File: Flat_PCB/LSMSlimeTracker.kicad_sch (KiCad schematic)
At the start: 49 parts, among them J1 USB_C_Receptacle_USB2.0, J2 Conn_01x04_Socket, Q1 Q_PMOS_GSD, SW1 SW_Push, SW2 SW_SPDT, SW3 SW_Push, U1 LSM6DSV16X, U2 M3406, U3 ESP32-C3-WROOM-02-N4, U7 BQ24040DSQT

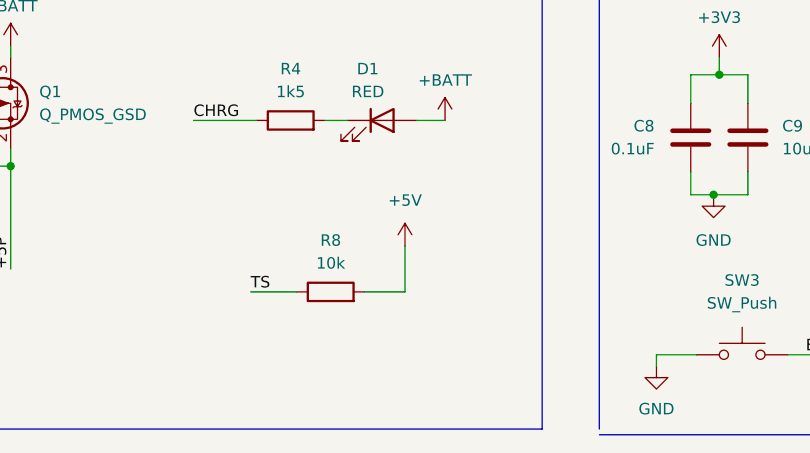
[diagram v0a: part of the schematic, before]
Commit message: TTDM fix
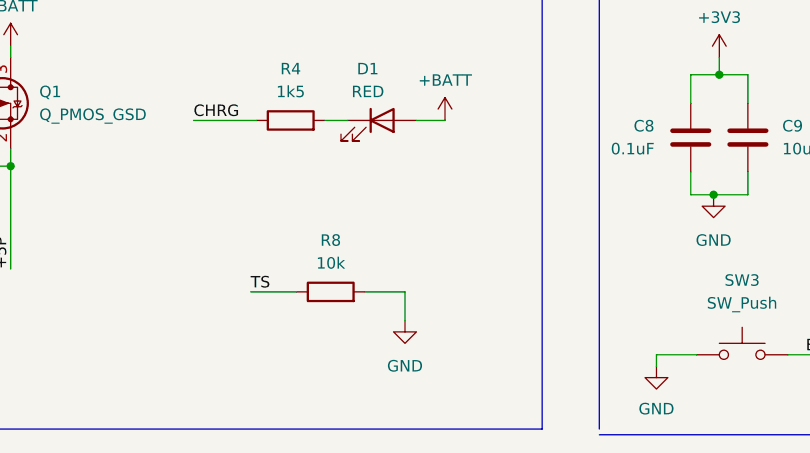
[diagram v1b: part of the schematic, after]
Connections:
- net +5V: no longer R8.2
- net GND: now also R8.2
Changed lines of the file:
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@@
-    (stroke (width 0) (type default))
-  )
-  (wire (pts (xy 196.85 180.34) (xy 196.85 185.42))
     (stroke (width 0) (type default))
   )
@@
   )
   (polyline (pts (xy 212.09 200.66) (xy 212.09 17.78))
+    (stroke (width 0) (type default))
+  )
+  (wire (pts (xy 196.85 185.42) (xy 196.85 188.595))
     (stroke (width 0) (type default))
   )
@@
         (path "/c06b72f6-429a-4daf-bf10-b679f7f09670"
           (reference "#PWR021") (unit 1)
-        )
-      )
-    )
-  )
-  (symbol (lib_id "power:+5V") (at 196.85 180.34 0) (unit 1)
-    (in_bom yes) (on_board yes) (dnp no) (fields_autoplaced)
-    (property "Reference" "#PWR017" (at 196.85 184.15 0)
-      (effects (font (size 1.27 1.27)) hide)
-    )
-    (property "Value" "+5V" (at 196.85 175.26 0)
-      (effects (font (size 1.27 1.27)))
-    )
-    (property "Footprint" "" (at 196.85 180.34 0)
-      (effects (font (size 1.27 1.27)) hide)
-    )
-    (property "Datasheet" "" (at 196.85 180.34 0)
-      (effects (font (size 1.27 1.27)) hide)
-    )
-    (pin "1")
-    (instances
-      (project "LSMSlimeTracker"
-        (path "/c06b72f6-429a-4daf-bf10-b679f7f09670"
-          (reference "#PWR017") (unit 1)
         )
       )
@@
         )
       )
+    )
+  )
+  (symbol (lib_id "power:GND") (at 196.85 188.595 0) (unit 1)
+    (in_bom yes) (on_board yes) (dnp no) (fields_autoplaced)
+    (property "Reference" "#PWR017" (at 196.85 194.945 0)
+      (effects (font (size 1.27 1.27)) hide)
+    )
+    (property "Value" "GND" (at 196.85 193.675 0)
+      (effects (font (size 1.27 1.27)))
+    )
+    (property "Footprint" "" (at 196.85 188.595 0)
+      (effects (font (size 1.27 1.27)) hide)
+    )
+    (property "Datasheet" "" (at 196.85 188.595 0)
+      (effects (font (size 1.27 1.27)) hide)
+    )
+    (pin "1")
+    (instances
+      (project "LSMSlimeTracker"
+        (path "/c06b72f6-429a-4daf-bf10-b679f7f09670"
+          (reference "#PWR017") (unit 1)
+        )
+      )

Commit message: V1.2
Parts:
- removed C4: 4.7uF, Capacitor_SMD:C_0603_1608Metric, symbol Device:C
- removed R1, R21: 10k, Resistor_SMD:R_0603_1608Metric, symbol Device:R
- removed R12: 100k, Resistor_SMD:R_0603_1608Metric, symbol Device:R
- removed R13: 180k, Resistor_SMD:R_0603_1608Metric, symbol Device:R
- removed R20, R22: 5k1, Resistor_SMD:R_0603_1608Metric, symbol Device:R
- removed R4: 1k5, Resistor_SMD:R_0603_1608Metric, symbol Device:R
- added C6: 10uF, Capacitor_SMD:C_0603_1608Metric, symbol Device:C
- added R10, R15, R17: 150k, Resistor_SMD:R_0603_1608Metric, symbol Device:R
- added R14, R16, R18, R6: 10k, Resistor_SMD:R_0603_1608Metric, symbol Device:R
- added R9: 2k, Resistor_SMD:R_0603_1608Metric, symbol Device:R
- R11: value 220k -> 150k; MPN C25767 -> C25755
- R5: value 1k5 -> 150k; MPN C25867 -> C25755
- R7: value 100k -> 2k; MPN C25741 -> C4109
- R8: value 10k -> 5k1; MPN C25744 -> C25905
- TP1: renamed from TP2; now left out of the parts list
- TP2: renamed from TP1; now left out of the parts list
- TP3: renamed from TP7; now left out of the parts list
- TP4: renamed from TP5; now left out of the parts list
- TP5: renamed from TP6; now left out of the parts list
- TP6: renamed from TP3; now left out of the parts list
- TP7: renamed from TP4; now left out of the parts list
- U1: footprint LGA_Custom:LGA14L_LSM6_STM -> LGA_Custom:Bosch_LGA-14_3x2.5mm_P0.5mm
- U2: renamed from U7; footprint SON40P200X200X80-11N -> SON_Custom:SON40P200X200X80-11N
- U3: footprint MODULE_ESP32-C3-WROOM-02-H4 -> ESP_Custom:MODULE_ESP32-C3-WROOM-02-H4
- renumbered C2 to C1, C1 to C2, C11 to C3, C12 to C4, C8 to C5, C9 to C7, C3 to C8, C5 to C9, D2 to D1, D1 to D2, J2 to J1, J1 to J2, R9 to R1, R3 to R12, R6 to R13, R10 to R2, R18 to R3, R19 to R4, SW2 to SW1, SW3 to SW2, SW1 to SW3, U2 to U4
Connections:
- net +3V3: now also R8.1, R14.2, R16.2, R18.2
- net +5V: now also R5.2; no longer R7.1
- net ADC: now also R11.1, R10.2, R15.1; no longer R11.2
- net CHRG: now also R7.1
- net EN: now also R18.1
- net GND: now also R11.2, R5.1, C6.2, R10.1, R6.1; no longer R7.2, R8.2
- net GPIO0: now also R9.1; no longer R5.1
- net SCL: now also R14.1
- net SDA: now also R16.1
- net VCC: now also C6.1, R17.2
- net at D3.1 (K): now also R9.2; no longer R5.2
- net at D2.1 (K): now also R7.2
- net at U3.16 (IO2): now also R8.2
- net TS: no longer names the net of U2.9 (TS)
- net TS: now also R6.2; no longer R8.1
- new net: R15.2, R17.1
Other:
- moved on the sheet: C3, C4, R3, R4, SW1
